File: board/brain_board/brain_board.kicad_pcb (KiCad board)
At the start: 2 copper layers, 77 x 63 mm, 9 parts, among them J1 Screw_Terminal_01x03, J2 Conn_02x04_Odd_Even, J3 Micro_SD_Card, M1 MountingHoles, U1 WeMos_D1_mini, U2 TAD3-0303-WEDI

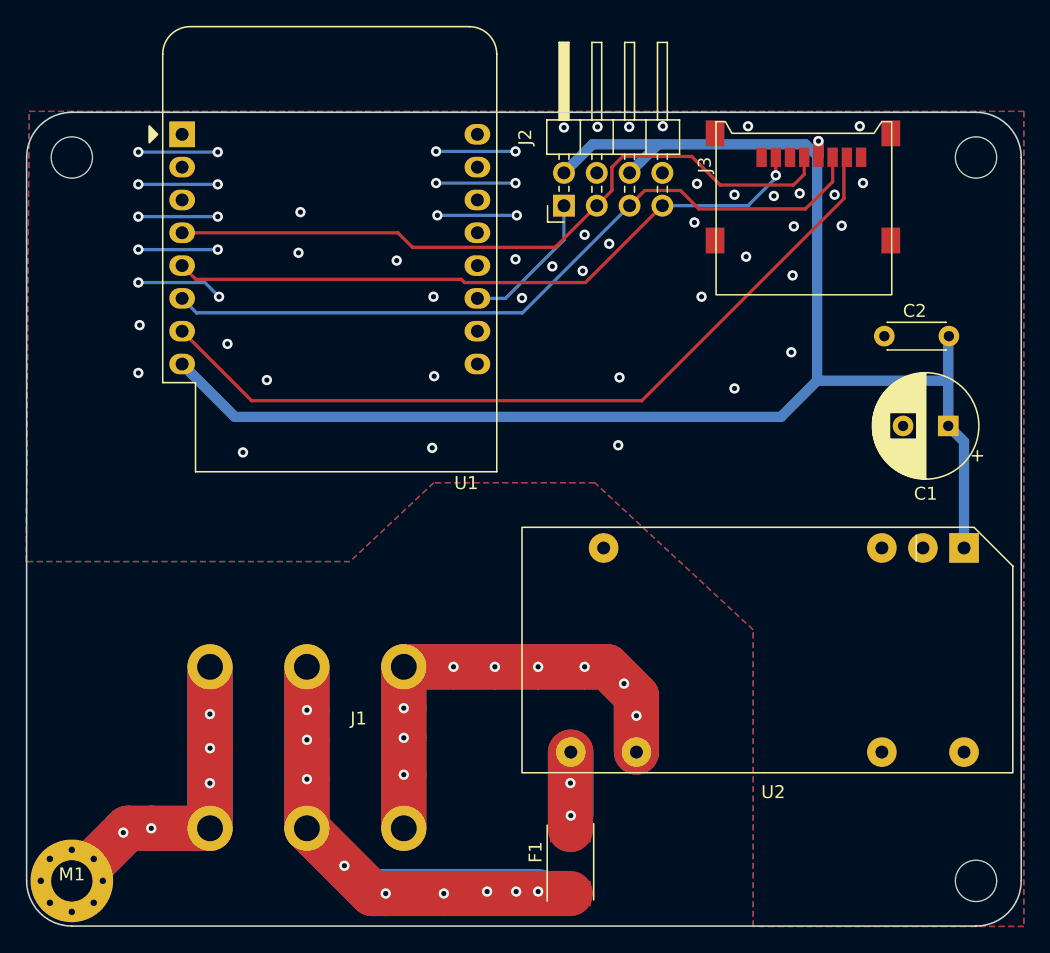
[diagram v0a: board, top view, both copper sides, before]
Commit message: Fix SD-Slot pin alignment
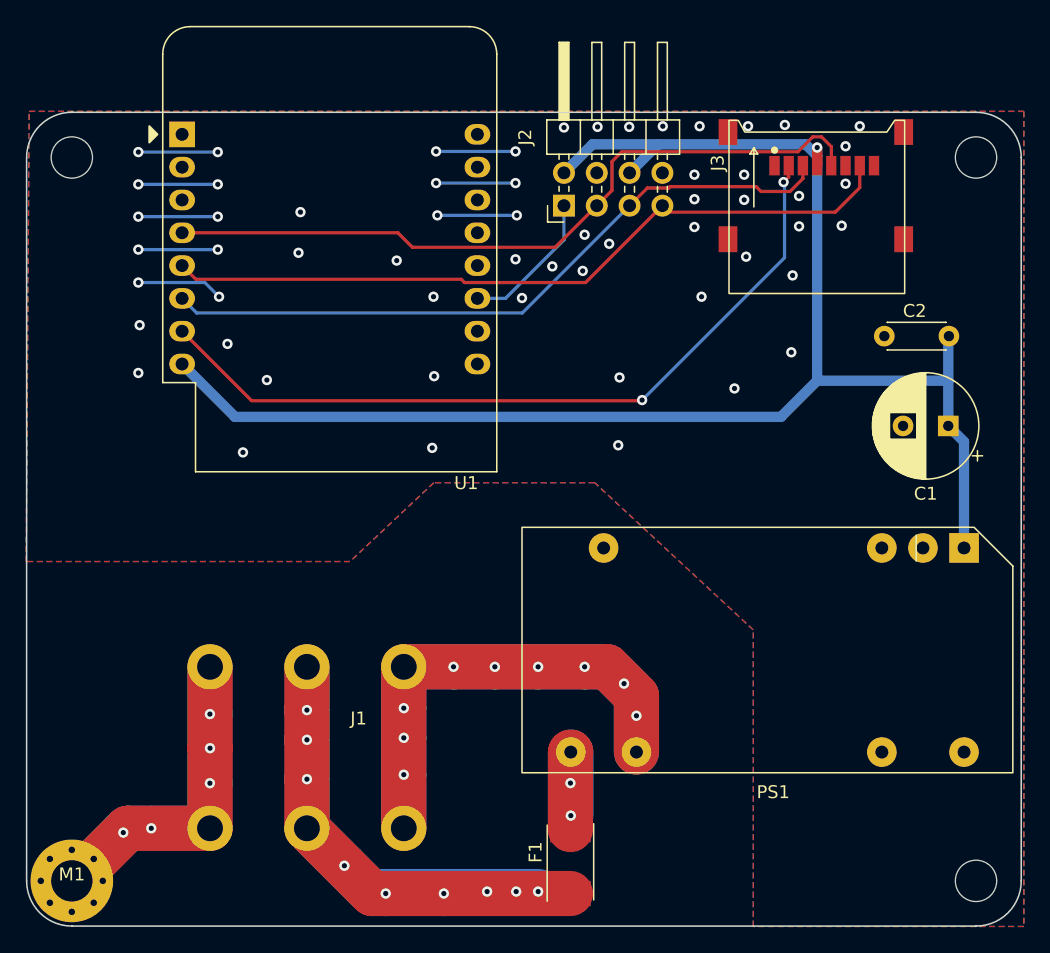
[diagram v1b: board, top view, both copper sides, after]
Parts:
- moved J3 1.00 mm to (171.3, 52.2)
- renumbered U2 to PS1
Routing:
- net MISO: track 51.5 -> 58.2 mm, vias 1 -> 0
- net MOSI: track 58.1 -> 54.1 mm
- net SD_CS: track 63.2 -> 60.8 mm, vias 0 -> 2
- net CLK: track 55.2 -> 57.4 mm
- net GND: vias 55 -> 58
